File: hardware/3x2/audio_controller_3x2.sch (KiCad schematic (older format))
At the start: 7 parts

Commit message: teensy -> 3x2.
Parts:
- C? (x4): footprint footprints:SM1210 -> audio_controller_3x2:SM1210
- MDT1: footprint audio_controller_teensy:MODULAR_DEVICE_TEENSY_MALE -> audio_controller_3x2:MODULAR_DEVICE_TEENSY_MALE
- U?: footprint footprints:QFN-5x5-32 -> audio_controller_3x2:QFN-5x5-32
- U?: footprint footprints:SOT-23-3 -> audio_controller_3x2:SOT-23-3
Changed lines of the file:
@@
 LIBS:valves
 LIBS:components
-LIBS:audio_controller_teensy
+LIBS:audio_controller_3x2
 EELAYER 25 0
 EELAYER END
@@
 encoding utf-8
 Sheet 1 1
-Title "audio_controller_teensy"
+Title "audio_controller_3x2"
 Date ""
 Rev "1.0"
@@
 F 0 "MDT1" H 2600 2597 60  0000 C CNN
 F 1 "MODULAR_DEVICE_TEENSY_MALE" H 2600 2491 60  0000 C CNN
-F 2 "audio_controller_teensy:MODULAR_DEVICE_TEENSY_MALE" H 2600 2650 60  0001 C CNN
+F 2 "audio_controller_3x2:MODULAR_DEVICE_TEENSY_MALE" H 2600 2650 60  0001 C CNN
 F 3 "" H 2650 4350 60  0000 C CNN
 F 4 "digikey" H 2600 2750 60  0001 C CNN "Vendor"
@@
 F 0 "U?" H 7800 3000 60  0000 C CNN
 F 1 "SGTL5000" H 6950 3000 60  0000 C CNN
-F 2 "footprints:QFN-5x5-32" H 7650 2900 60  0001 C CNN
+F 2 "audio_controller_3x2:QFN-5x5-32" H 7650 2900 60  0001 C CNN
 F 3 "" H 7350 2300 60  0001 C CNN
 F 4 "digikey" H 7850 3100 60  0001 C CNN "Vendor"
@@
 F 0 "U?" H 2400 3847 60  0000 C CNN
 F 1 "AP7313_1.5V" H 2400 3741 60  0000 C CNN
-F 2 "footprints:SOT-23-3" H 2450 3300 60  0001 C CNN
+F 2 "audio_controller_3x2:SOT-23-3" H 2450 3300 60  0001 C CNN
 F 3 "" H 2400 3600 60  0001 C CNN
 F 4 "digikey" H 2650 3500 60  0001 C CNN "Vendor"
@@
 F 0 "C?" H 1650 3950 40  0000 L CNN
 F 1 "2.2uF" H 1600 3850 30  0000 C CNN
-F 2 "footprints:SM1210" H 1638 3700 30  0001 C CNN
+F 2 "audio_controller_3x2:SM1210" H 1638 3700 30  0001 C CNN
 F 3 "" H 1600 3850 60  0000 C CNN
 F 4 "digikey" H 1700 4050 60  0001 C CNN "Vendor"
@@
 F 0 "C?" H 1850 3950 40  0000 L CNN
 F 1 "0.1uF" H 1800 3850 30  0000 C CNN
-F 2 "footprints:SM1210" H 1838 3700 30  0001 C CNN
+F 2 "audio_controller_3x2:SM1210" H 1838 3700 30  0001 C CNN
 F 3 "" H 1800 3850 60  0000 C CNN
 F 4 "digikey" H 1900 4050 60  0001 C CNN "Vendor"
@@
 F 0 "C?" H 2050 3950 40  0000 L CNN
 F 1 "0.1uF" H 2000 3850 30  0000 C CNN
-F 2 "footprints:SM1210" H 2038 3700 30  0001 C CNN
+F 2 "audio_controller_3x2:SM1210" H 2038 3700 30  0001 C CNN
 F 3 "" H 2000 3850 60  0000 C CNN
 F 4 "digikey" H 2100 4050 60  0001 C CNN "Vendor"
@@
 F 0 "C?" H 2950 3950 40  0000 L CNN
 F 1 "2.2uF" H 2900 3850 30  0000 C CNN
-F 2 "footprints:SM1210" H 2938 3700 30  0001 C CNN
+F 2 "audio_controller_3x2:SM1210" H 2938 3700 30  0001 C CNN
 F 3 "" H 2900 3850 60  0000 C CNN
 F 4 "digikey" H 3000 4050 60  0001 C CNN "Vendor"

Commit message: Schematic progress.
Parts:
- added C?: 2.2uF, audio_controller_3x2:SM1210, symbol 2.2uF
- added C?: 0.1uF, audio_controller_3x2:SM1210, symbol 0.1uF
- added L?: 600@100MHz, footprints:SM1210, symbol 600@100MHz
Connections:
- net +3V3: now also C?.1, C?.1, C?.1, U?.1 (IN), U?.20 (VDIO), L?.1
- net BCLK: now also U?.24 (I2S_SCLK)
- net GND: now also C?.2, C?.2, C?.2, C?.2, U?.1 (GND), U?.3 (GND), U?.3 (GND), U?.31 (CTRL_ADR0_CS), U?.32 (CTRL_MODE), U?.4 (HP_VGND), U?.7 (AGND), U?.PAD (GND), C?.2, C?.2
- net I2SRX: now also U?.25 (I2S_DOUT)
- net I2STX: now also U?.26 (I2S_DIN)
- net LRCLK: now also U?.23 (I2S_LRCLK)
- net MCLK: now also U?.21 (SYS_MCLK)
- net SCL: now also U?.29 (CTRL_CLK)
- net SDA: now also U?.27 (CTRL_DATA)
- net +1V5: now reaches U?.30 (VDDD)
- net +1V5: now also C?.1, U?.2 (OUT)
- net at U?.5 (VDDA): now also C?.1, C?.1, L?.2
- no-connect marks 17 -> 18
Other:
- moved on the sheet: C?, U?

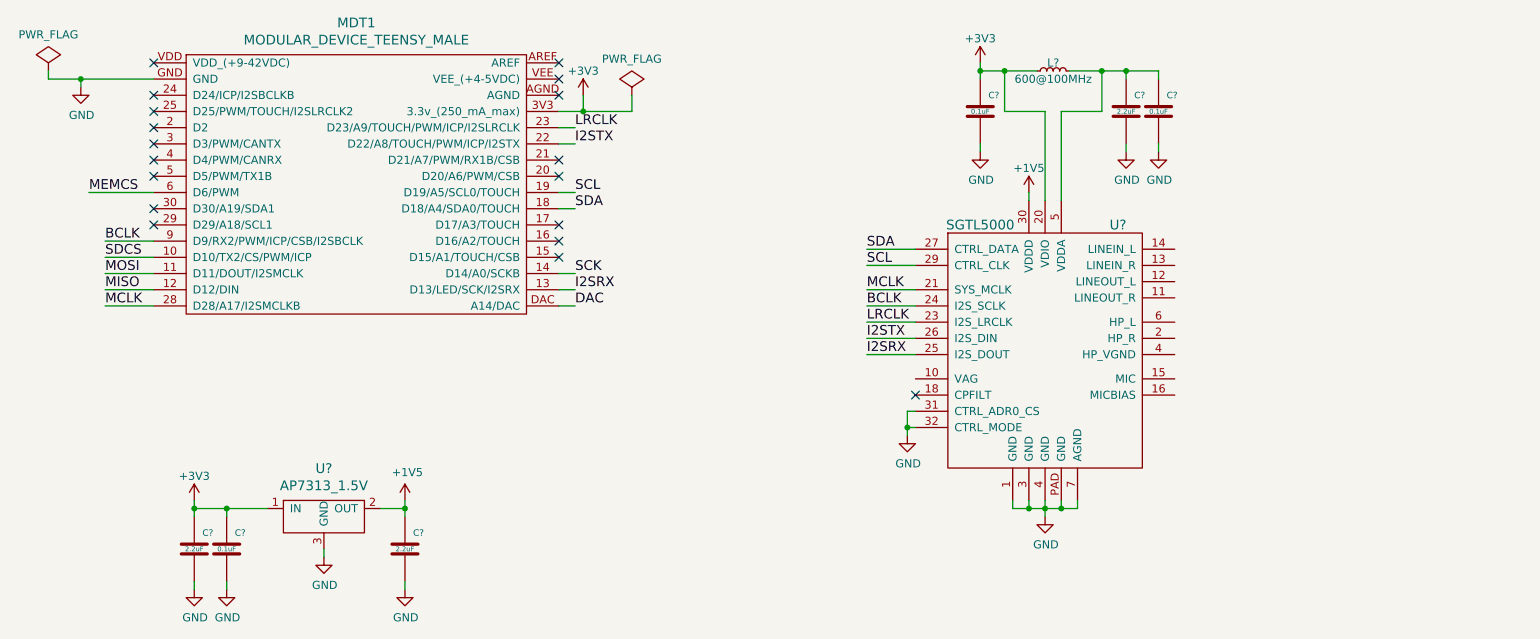
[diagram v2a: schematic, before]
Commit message: Added headphone jack.
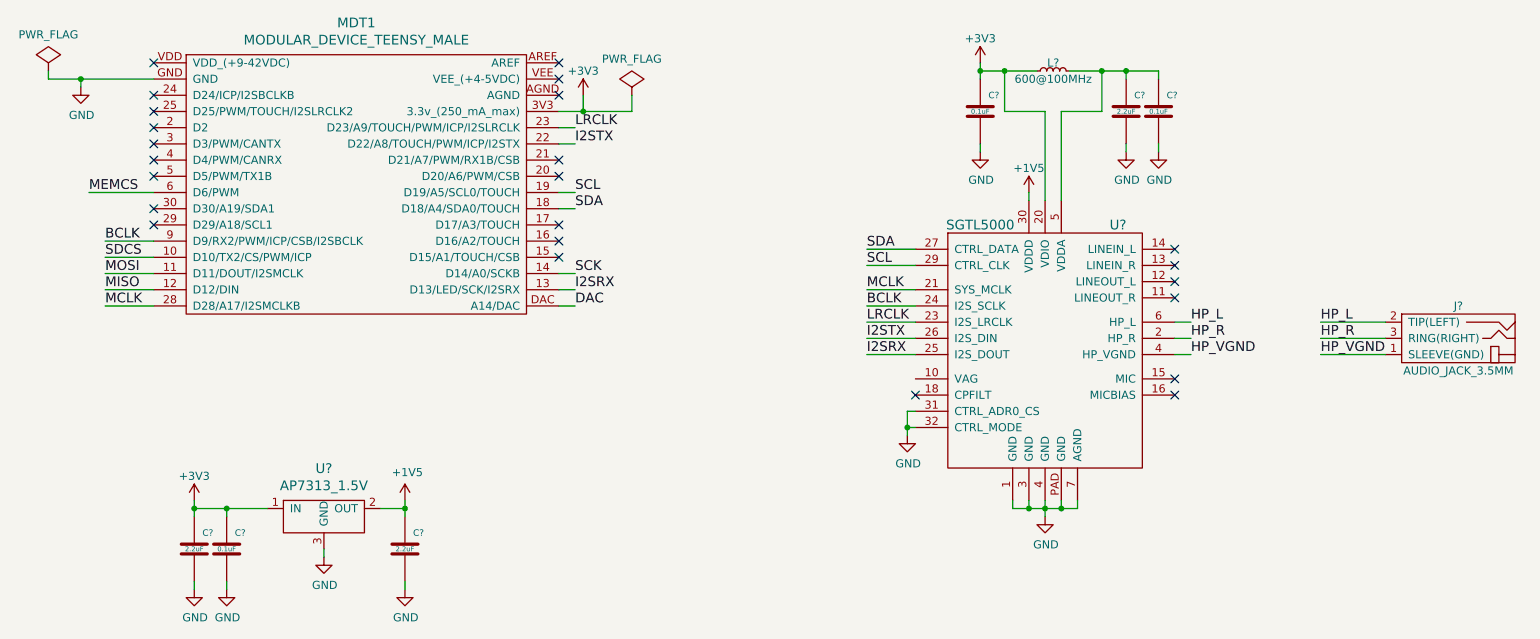
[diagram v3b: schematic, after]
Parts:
- added J?: AUDIO_JACK_3.5MM, audio_controller_3x2:AUDIO_JACK_3.5MM_3PIN, symbol AUDIO_JACK_3.5MM
- L?: footprint footprints:SM1210 -> audio_controller_3x2:SM1210
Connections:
- net HP_R: now reaches U?.2 (HP_R)
- net HP_R: now also J?.3 (RING(RIGHT))
- net HP_VGND: now reaches U?.4 (HP_VGND)
- net HP_VGND: now also J?.1 (SLEEVE(GND))
- net HP_L: now reaches U?.6 (HP_L)
- net HP_L: now also J?.2 (TIP(LEFT))
- no-connect marks 18 -> 24
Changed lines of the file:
@@
 	900  1000 900  950
 Wire Wire Line
-	700  950  1350 950
+	700  950  900  950
+Wire Wire Line
+	900  950  1350 950
 NoConn ~ 3850 850
 NoConn ~ 3850 1050
@@
 	4300 1150 4300 1050
 Wire Wire Line
-	3850 1150 4300 1150
+	3850 1150 4000 1150
+Wire Wire Line
+	4000 1150 4300 1150
 Wire Wire Line
 	4000 1050 4000 1150
@@
 $EndComp
 Wire Wire Line
-	1600 3550 1600 3650
-Wire Wire Line
-	1600 3600 2050 3600
+	1600 3550 1600 3600
+Wire Wire Line
+	1600 3600 1600 3650
+Wire Wire Line
+	1600 3600 1800 3600
+Wire Wire Line
+	1800 3600 2050 3600
 Wire Wire Line
 	1800 3650 1800 3600
@@
 	2750 3600 2900 3600
 Wire Wire Line
-	2900 3550 2900 3650
+	2900 3550 2900 3600
+Wire Wire Line
+	2900 3600 2900 3650
 $Comp
 L +3V3 #PWR?
@@
 F 0 "L?" V 6950 900 50  0000 C CNN
 F 1 "600@100MHz" V 6850 900 50  0000 C CNN
-F 2 "footprints:SM1210" H 6830 840 50  0001 C CNN
+F 2 "audio_controller_3x2:SM1210" H 6830 840 50  0001 C CNN
 F 3 "" H 6900 900 50  0000 C CNN
 F 4 "digikey" H 7030 1040 60  0001 C CNN "Vendor"
@@
 $EndComp
 Wire Wire Line
-	6450 850  6450 950
-Wire Wire Line
-	6450 900  6800 900
-Wire Wire Line
-	7000 900  7550 900
+	6450 850  6450 900
+Wire Wire Line
+	6450 900  6450 950
+Wire Wire Line
+	6450 900  6600 900
+Wire Wire Line
+	6600 900  6800 900
+Wire Wire Line
+	7000 900  7200 900
+Wire Wire Line
+	7200 900  7350 900
+Wire Wire Line
+	7350 900  7550 900
 Wire Wire Line
 	7550 900  7550 950
@@
 	6650 3550 6650 3600
 Wire Wire Line
-	6650 3600 7050 3600
+	6650 3600 6750 3600
+Wire Wire Line
+	6750 3600 6850 3600
+Wire Wire Line
+	6850 3600 6950 3600
+Wire Wire Line
+	6950 3600 7050 3600
 Wire Wire Line
 	7050 3600 7050 3550
@@
 Connection ~ 6750 3600
 Wire Wire Line
-	6850 3550 6850 3650
+	6850 3550 6850 3600
+Wire Wire Line
+	6850 3600 6850 3650
 Connection ~ 6850 3600
 Wire Wire Line
@@
 	6050 3000 6000 3000
 Wire Wire Line
-	6000 3000 6000 3150
+	6000 3000 6000 3100
+Wire Wire Line
+	6000 3100 6000 3150
 Wire Wire Line
 	6050 3100 6000 3100
 Connection ~ 6000 3100
+NoConn ~ 7650 2800
+NoConn ~ 7650 2900
+NoConn ~ 7650 2000
+NoConn ~ 7650 2100
+NoConn ~ 7650 2200
+NoConn ~ 7650 2300
+$Comp
+L AUDIO_JACK_3.5MM J?
+U 1 1 5817680D
+P 9400 2550
+F 0 "J?" H 9400 2750 50  0000 C CNN
+F 1 "AUDIO_JACK_3.5MM" H 9400 2350 50  0000 C CNN
+F 2 "audio_controller_3x2:AUDIO_JACK_3.5MM_3PIN" H 9300 2650 50  0001 C CNN
+F 3 "" H 9400 2550 50  0000 C CNN
+F 4 "digikey" H 9500 2850 60  0001 C CNN "Vendor"
+F 5 "CP-3523SJCT-ND" H 9600 2950 60  0001 C CNN "PartNumber"
+F 6 "3.50mm Headphone Phone Jack Stereo Connector Solder" H 9700 3050 60  0001 C CNN "Description"
+	1    9400 2550
+	1    0    0    -1
+$EndComp
+Wire Wire Line
+	7650 2450 7750 2450
+Wire Wire Line
+	7650 2550 7750 2550
+Wire Wire Line
+	7650 2650 7750 2650
+Text Label 7750 2450 0    60   ~ 0
+HP_L
+Text Label 7750 2550 0    60   ~ 0
+HP_R
+Text Label 7750 2650 0    60   ~ 0
+HP_VGND
+Wire Wire Line
+	8950 2450 8550 2450
+Wire Wire Line
+	8950 2550 8550 2550
+Wire Wire Line
+	8950 2650 8550 2650
+Text Label 8550 2450 0    60   ~ 0
+HP_L
+Text Label 8550 2550 0    60   ~ 0
+HP_R
+Text Label 8550 2650 0    60   ~ 0
+HP_VGND
 $EndSCHEMATC

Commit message: Added pullup resistors.
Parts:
- added C?: 0.15uF, footprints:SM1210, symbol 0.15uF
- added R? (x2): 2.21k, footprints:SM1210, symbol 2.21k
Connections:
- net +3V3: now also R?.1, R?.1
- net GND: now also C?.2
- net SCL: now also R?.2
- net SDA: now also R?.2
- net at U?.10 (VAG): now also C?.1
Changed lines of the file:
@@
 	900  1000 900  950
 Wire Wire Line
-	700  950  900  950
-Wire Wire Line
-	900  950  1350 950
+	700  950  1350 950
 NoConn ~ 3850 850
 NoConn ~ 3850 1050
@@
 	4300 1150 4300 1050
 Wire Wire Line
-	3850 1150 4000 1150
-Wire Wire Line
-	4000 1150 4300 1150
+	3850 1150 4300 1150
 Wire Wire Line
 	4000 1050 4000 1150
@@
 $EndComp
 Wire Wire Line
-	1600 3550 1600 3600
-Wire Wire Line
-	1600 3600 1600 3650
-Wire Wire Line
-	1600 3600 1800 3600
-Wire Wire Line
-	1800 3600 2050 3600
+	1600 3550 1600 3650
+Wire Wire Line
+	1600 3600 2050 3600
 Wire Wire Line
 	1800 3650 1800 3600
@@
 	2750 3600 2900 3600
 Wire Wire Line
-	2900 3550 2900 3600
-Wire Wire Line
-	2900 3600 2900 3650
+	2900 3550 2900 3650
 $Comp
 L +3V3 #PWR?
@@
 $EndComp
 Wire Wire Line
-	6450 850  6450 900
-Wire Wire Line
-	6450 900  6450 950
-Wire Wire Line
-	6450 900  6600 900
-Wire Wire Line
-	6600 900  6800 900
-Wire Wire Line
-	7000 900  7200 900
-Wire Wire Line
-	7200 900  7350 900
-Wire Wire Line
-	7350 900  7550 900
+	6450 850  6450 950
+Wire Wire Line
+	6450 900  6800 900
+Wire Wire Line
+	7000 900  7550 900
 Wire Wire Line
 	7550 900  7550 950
@@
 	6650 3550 6650 3600
 Wire Wire Line
-	6650 3600 6750 3600
-Wire Wire Line
-	6750 3600 6850 3600
-Wire Wire Line
-	6850 3600 6950 3600
-Wire Wire Line
-	6950 3600 7050 3600
+	6650 3600 7050 3600
 Wire Wire Line
 	7050 3600 7050 3550
@@
 Connection ~ 6750 3600
 Wire Wire Line
-	6850 3550 6850 3600
-Wire Wire Line
-	6850 3600 6850 3650
+	6850 3550 6850 3650
 Connection ~ 6850 3600
 Wire Wire Line
@@
 	6050 3000 6000 3000
 Wire Wire Line
-	6000 3000 6000 3100
-Wire Wire Line
-	6000 3100 6000 3150
+	6000 3000 6000 3150
 Wire Wire Line
 	6050 3100 6000 3100
@@
 Text Label 8550 2650 0    60   ~ 0
 HP_VGND
+$Comp
+L 0.15uF C?
+U 1 1 5818C7AA
+P 5750 3050
+F 0 "C?" H 5800 3150 40  0000 L CNN
+F 1 "0.15uF" H 5750 3050 30  0000 C CNN
+F 2 "footprints:SM1210" H 5788 2900 30  0001 C CNN
+F 3 "" H 5750 3050 60  0000 C CNN
+F 4 "digikey" H 5850 3250 60  0001 C CNN "Vendor"
+F 5 "399-11615-1-ND" H 5950 3350 60  0001 C CNN "PartNumber"
+F 6 "0.15uF 100V Ceramic Capacitor X7R 1210" H 6050 3450 60  0001 C CNN "Description"
+	1    5750 3050
+	1    0    0    -1
+$EndComp
+$Comp
+L GND #PWR?
+U 1 1 5818C9D7
+P 5750 3300
+F 0 "#PWR?" H 5750 3050 50  0001 C CNN
+F 1 "GND" H 5755 3127 50  0000 C CNN
+F 2 "" H 5750 3300 50  0000 C CNN
+F 3 "" H 5750 3300 50  0000 C CNN
+	1    5750 3300
+	1    0    0    -1
+$EndComp
+Wire Wire Line
+	5750 2850 5750 2800
+Wire Wire Line
+	5750 2800 6050 2800
+Wire Wire Line
+	5750 3250 5750 3300
+$Comp
+L 2.21k R?
+U 1 1 5818DFC6
+P 5050 1200
+F 0 "R?" V 4950 1200 40  0000 C CNN
+F 1 "2.21k" V 5050 1200 40  0000 C CNN
+F 2 "footprints:SM1210" V 4980 1200 30  0001 C CNN
+F 3 "" H 5050 1200 30  0000 C CNN
+F 4 "digikey" V 5230 1300 60  0001 C CNN "Vendor"
+F 5 "P2.21KAACT-ND" V 5330 1400 60  0001 C CNN "PartNumber"
+F 6 "RES SMD 2.21K OHM 1% 1/2W 1210" V 5430 1500 60  0001 C CNN "Description"
+	1    5050 1200
+	1    0    0    -1
+$EndComp
+$Comp
+L 2.21k R?
+U 1 1 5818E533
+P 5250 1200
+F 0 "R?" V 5150 1200 40  0000 C CNN
+F 1 "2.21k" V 5250 1200 40  0000 C CNN
+F 2 "footprints:SM1210" V 5180 1200 30  0001 C CNN
+F 3 "" H 5250 1200 30  0000 C CNN
+F 4 "digikey" V 5430 1300 60  0001 C CNN "Vendor"
+F 5 "P2.21KAACT-ND" V 5530 1400 60  0001 C CNN "PartNumber"
+F 6 "RES SMD 2.21K OHM 1% 1/2W 1210" V 5630 1500 60  0001 C CNN "Description"
+	1    5250 1200
+	1    0    0    -1
+$EndComp
+Wire Wire Line
+	5250 1450 5250 1500
+Wire Wire Line
+	5250 1500 5300 1500
+Wire Wire Line
+	5050 1450 5050 1600
+Wire Wire Line
+	5050 1600 5300 1600
+Text Label 5300 1600 0    60   ~ 0
+SDA
+Text Label 5300 1500 0    60   ~ 0
+SCL
+$Comp
+L +3V3 #PWR?
+U 1 1 5818E70A
+P 5050 900
+F 0 "#PWR?" H 5050 750 50  0001 C CNN
+F 1 "+3V3" H 5050 1050 50  0000 C CNN
+F 2 "" H 5050 900 50  0000 C CNN
+F 3 "" H 5050 900 50  0000 C CNN
+	1    5050 900
+	1    0    0    -1
+$EndComp
+$Comp
+L +3V3 #PWR?
+U 1 1 5818E74D
+P 5250 900
+F 0 "#PWR?" H 5250 750 50  0001 C CNN
+F 1 "+3V3" H 5250 1050 50  0000 C CNN
+F 2 "" H 5250 900 50  0000 C CNN
+F 3 "" H 5250 900 50  0000 C CNN
+	1    5250 900
+	1    0    0    -1
+$EndComp
+Wire Wire Line
+	5050 900  5050 950
+Wire Wire Line
+	5250 900  5250 950
 $EndSCHEMATC
